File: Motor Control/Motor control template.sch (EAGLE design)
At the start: 1 part, among them X1 D-SUB25-H2M25ST

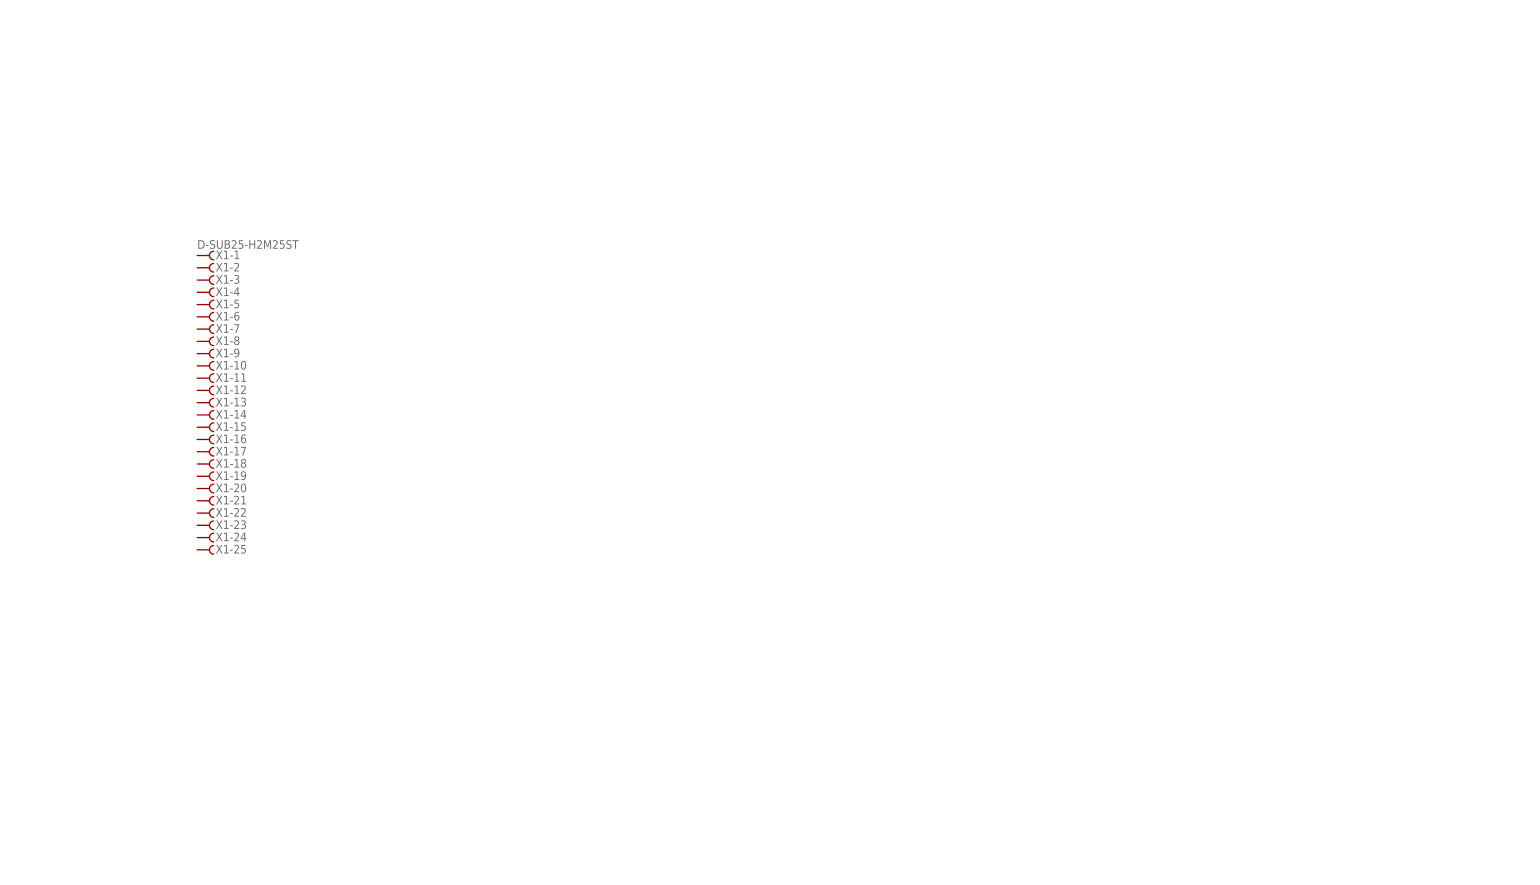
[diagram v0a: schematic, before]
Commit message: Started fleshing out motor control board v2, looking at spi option
Signed-off-by: Evan Milton <evan@bp2e.net>
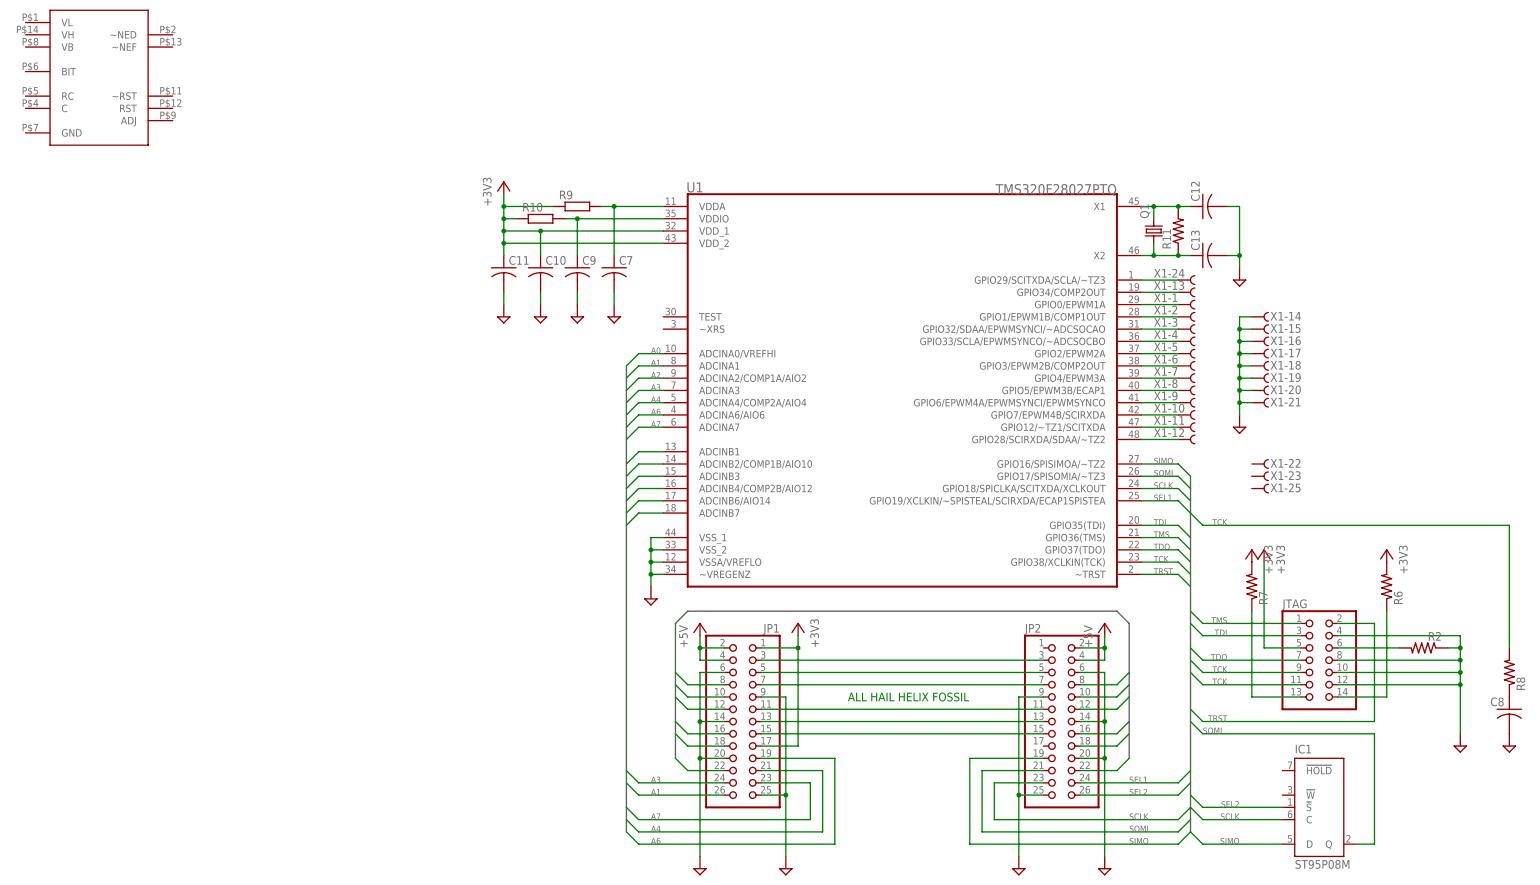
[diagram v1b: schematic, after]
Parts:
- added C10, C11, C12, C13, C7, C8, C9: (no value), resistor:C-USC0805
- added IC1: ST95P08M, st-microelectronics:ST95P08M
- added JP1, JP2: (no value), pinhead:PINHD-2X13
- added JTAG: (no value), pinhead:PINHD-2X7
- added Q1: (no value), crystal:CRYSTALHC49UP
- added R10, R9: (no value), rcl:R-EU_R0805
- added R11, R2, R6, R7, R8: (no value), rcl:R-US_M0805
- added U$1: HSN1000, RaspberryPi:HSN1000
- added U1: TMS320F28027PTQ, Texas Instruments_By_element14_Batch_1:TMS320F28027PTQ
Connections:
- new net +3V3: C10.1, C11.1, JP1.1, JP1.17, JTAG.5, R10.1, R6.2, R7.2, R9.1
- new net +5V: JP1.2, JP1.4, JP2.2, JP2.4
- new net A1: JP1.26
- new net A3: JP1.24
- new net A4: JP1.21
- new net A6: JP1.19
- new net A7: JP1.23
- new net DGND: C10.2, C11.2, C12.2, C13.2, C7.2, C8.2, C9.2, JP1.14, JP1.20, JP1.25, JP1.6, JP1.9, JP2.14, JP2.20, JP2.25, JP2.6, JP2.9, JTAG.10, JTAG.12, JTAG.4, JTAG.8, R2.1, X1-14.F, X1-15.F, X1-16.F, X1-17.F, X1-18.F, X1-19.F, X1-20.F, X1-21.F
- new net GPIO0: JP1.22, JP2.22
- new net GPIO1: JP1.18, JP2.18
- new net GPIO2: JP1.16, JP2.16
- new net GPIO3: JP1.12, JP2.12
- new net GPIO4: JP1.10, JP2.10
- new net GPIO5: JP1.8, JP2.8
- new net N$1: U1.GPIO0/EPWM1A, X1-1.F
- new net N$10: U1.GPIO5/EPWM3B/ECAP1, X1-8.F
- new net N$11: U1.GPIO6/EPWM4A/EPWMSYNCI/EPWMSYNCO, X1-9.F
- new net N$12: C8.1, R8.1
- new net N$13: JTAG.13, R7.1
- new net N$14: C7.1, R9.2
- new net N$15: C9.1, R10.2
- new net N$16: U1.GPIO7/EPWM4B/SCIRXDA, X1-10.F
- new net N$17: U1.GPIO12/~TZ1/SCITXDA, X1-11.F
- new net N$18: U1.GPIO28/SCIRXDA/SDAA/~TZ2, X1-12.F
- new net N$19: U1.GPIO29/SCITXDA/SCLA/~TZ3, X1-24.F
- new net N$2: U1.GPIO1/EPWM1B/COMP1OUT, X1-2.F
- new net N$20: U1.GPIO34/COMP2OUT, X1-13.F
- new net N$21: C12.1, Q1.2, R11.2, U1.X1
- new net N$22: C13.1, Q1.1, R11.1, U1.X2
- new net N$23: JP1.3, JP2.3
- new net N$24: JP1.5, JP2.5
- new net N$25: JP1.7, JP2.7
- new net N$26: JP1.11, JP2.11
- new net N$27: JP1.13, JP2.13
- new net N$28: JP1.15, JP2.15
- new net N$3: U1.GPIO32/SDAA/EPWMSYNCI/~ADCSOCAO, X1-3.F
- new net N$4: U1.GPIO33/SCLA/EPWMSYNCO/~ADCSOCBO, X1-4.F
- new net N$5: JTAG.14, R6.1
- new net N$6: JTAG.6, R2.2
- new net N$7: U1.GPIO2/EPWM2A, X1-5.F
- new net N$8: U1.GPIO3/EPWM2B/COMP2OUT, X1-6.F
- new net N$9: U1.GPIO4/EPWM3A, X1-7.F
- new net SCLK: IC1G$1.C, JP2.23, U1.GPIO18/SPICLKA/SCITXDA/XCLKOUT
- new net SEL1: JP2.24, U1.GPIO19/XCLKIN/~SPISTEAL/SCIRXDA/ECAP1SPISTEA
- new net SEL2: IC1G$1.!S, JP2.26
- new net SIMO: IC1G$1.D, JP2.19, U1.GPIO16/SPISIMOA/~TZ2
- new net SOMI: IC1G$1.Q, JP2.21, U1.GPIO17/SPISOMIA/~TZ3
- new net TCK: JTAG.11, JTAG.9, R8.2, U1.GPIO38/XCLKIN(TCK)
- new net TDI: JTAG.3, U1.GPIO35(TDI)
- new net TDO: JTAG.7, U1.GPIO37(TDO)
- new net TMS: JTAG.1, U1.GPIO36(TMS)
- new net TRST: JTAG.2, U1.~TRST
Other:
- note added: "ALL HAIL HELIX FOSSIL"
- moved on the sheet: X1-1, X1-10, X1-11, X1-12, X1-13, X1-14, X1-15, X1-16, X1-17, X1-18, X1-19, X1-2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
